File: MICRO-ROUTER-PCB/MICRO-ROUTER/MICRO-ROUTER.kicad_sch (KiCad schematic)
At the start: 72 parts, among them J2 USB_A, J3 USB_C_Receptacle_USB2.0_16P, J4 Battery Connector, J5 SPI Header, J6 GPIO Header, J7 RJ45 5-2301996-6, Q1 FS8205A, SW2 8Devices Reset, SW3 UART Reset, U1 TP4056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

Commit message: fixed reg
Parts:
- removed C9: 10uf, Capacitor_SMD:C_0603_1608Metric, symbol Device:C
- added L2: 4.7uf, Custom Footprints:INDPM5752X300N, symbol Device:L
- added U5: XC9141A50DMR-G, Custom Footprints:XC8107AC20MR-G, symbol Custom Symbols:XC9142B33DMR-G
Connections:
- net +5V: now also C7.1, U5.4 (Vout)
- net GND: now also U5.2 (GND)
- net V-UNREG: now also L2.2, U5.3 (BAT); no longer C7.1
- net V-UNREG SW: now reaches S1.2 (COM), U2.1 (CE)
- net V-UNREG SW: now also U5.1 (CE)
- new net: L2.1, U5.5 (LX)
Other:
- moved on the sheet: C1, C8, L1, S1, U2

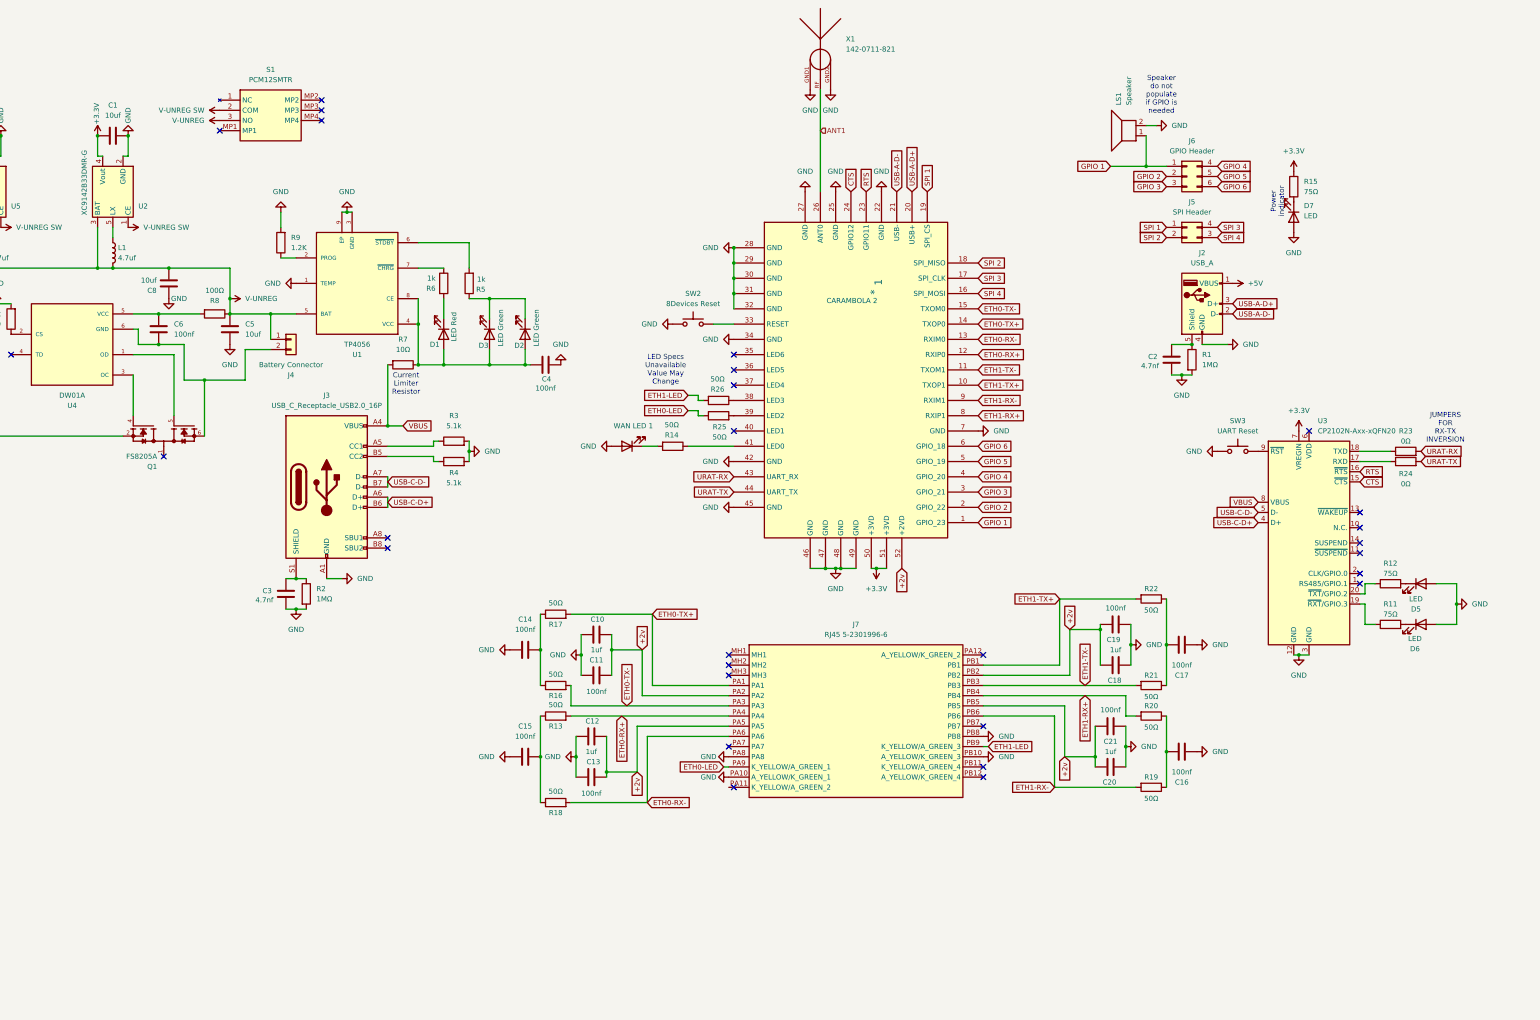
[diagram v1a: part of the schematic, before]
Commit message: -fixed all open issues in the schematic
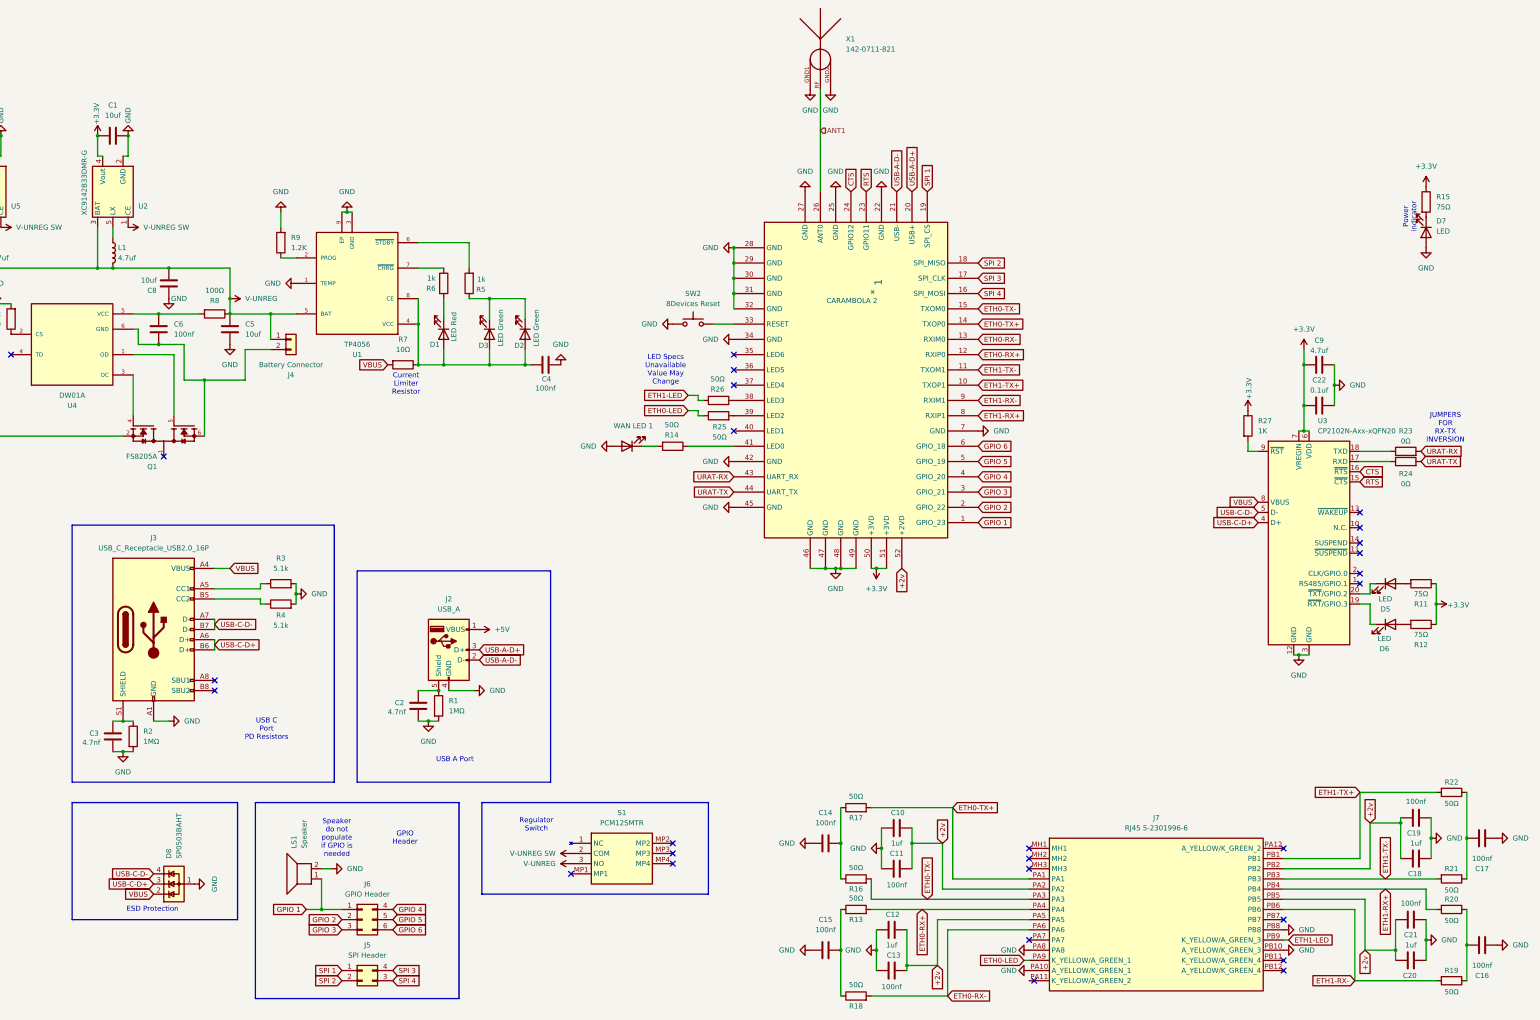
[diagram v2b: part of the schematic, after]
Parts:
- removed SW3: UART Reset, Button_Switch_THT:SW_PUSH_6mm, symbol Switch:SW_Push
- added C22: 0.1uf, symbol Device:C
- added C9: 4.7uf, symbol Device:C
- added D8: SP0503BAHT, Package_TO_SOT_SMD:SOT-143, symbol Power_Protection:SP0503BAHT
- added R27: 1K, Resistor_SMD:R_0603_1608Metric_Pad0.98x0.95mm_HandSolder, symbol Device:R
- J4: value Battery Connector -> Battery Connector
- U2: value XC9142B33DMR-G -> XC9142B33DMR-G
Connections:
- net +3.3V: now also R11.1, R12.1, U3.6 (VDD), C22.1, C9.1, R27.1
- net CTS: now also U3.16 (~{RTS}); no longer U3.15 (~{CTS})
- net GND: now also C22.2, C9.2, D8.1 (A); no longer D5.2 (A), D6.2 (A)
- net RTS: now also U3.15 (~{CTS}); no longer U3.16 (~{RTS})
- net USB-C-D+: now also D8.3 (K)
- net USB-C-D-: now also D8.4 (K)
- net VBUS: now also D8.2 (K)
- net at U3.9 (~{RST}): now also R27.2
- net at U3.19 (~{RXT}/GPIO.3): now also D6.1 (K); no longer R11.1
- net at R11.2: now also D5.2 (A); no longer D6.1 (K)
- net at U3.20 (~{TXT}/GPIO.2): now also D5.1 (K); no longer R12.1
- net at R12.2: now also D6.2 (A); no longer D5.1 (K)
- no-connect marks 28 -> 27
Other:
- note added: "ESD Protection"
- note added: "GPIO Header"
- note added: "Regulator Switch"
- note added: "USB A Port"
- note added: "USB C Port PD Resistors"
- moved on the sheet: C10, C11, C12, C13, C14, C15, C16, C17, C18, C19, C2, C20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

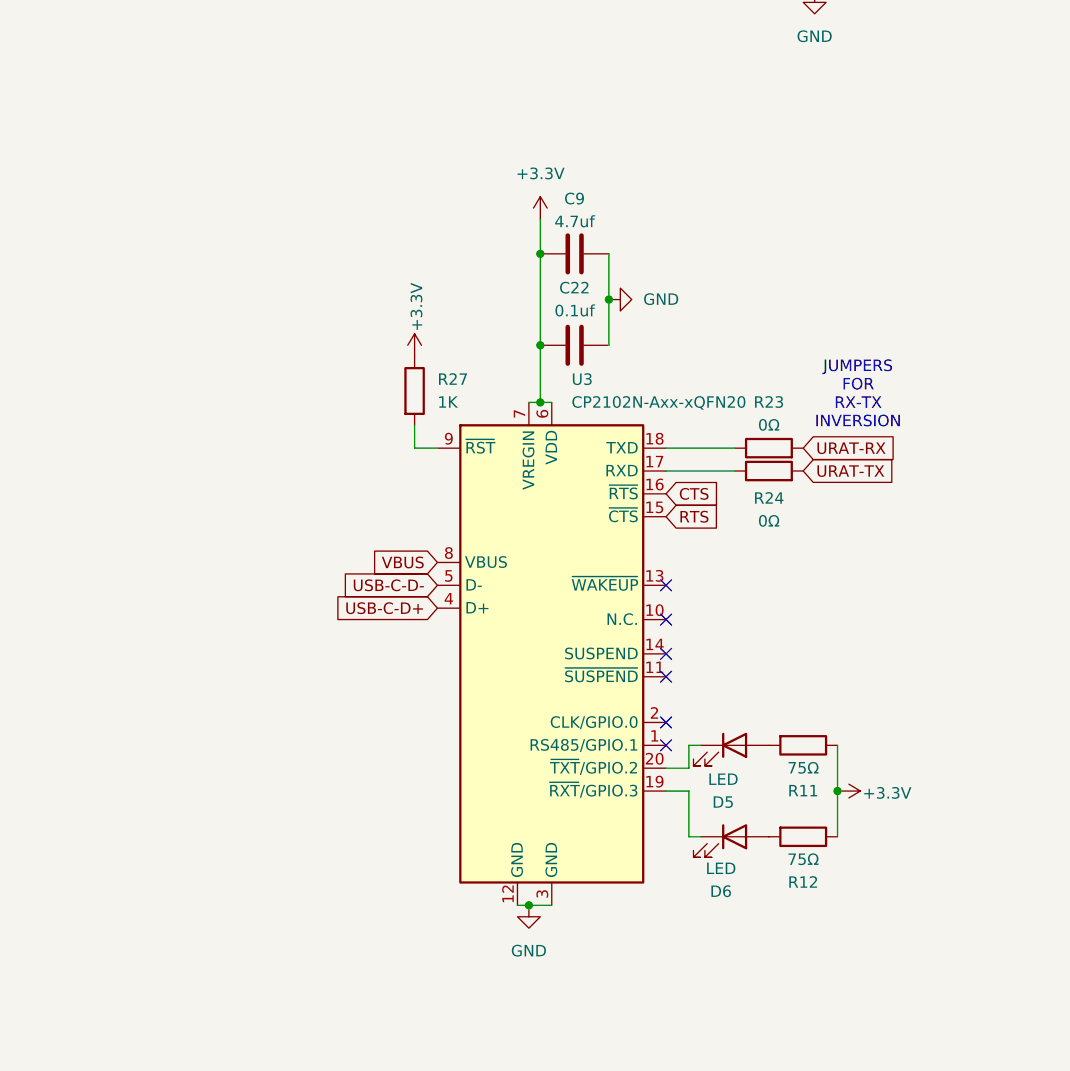
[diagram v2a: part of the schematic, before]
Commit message: -Fixed the ttl adapter (this time should be right)
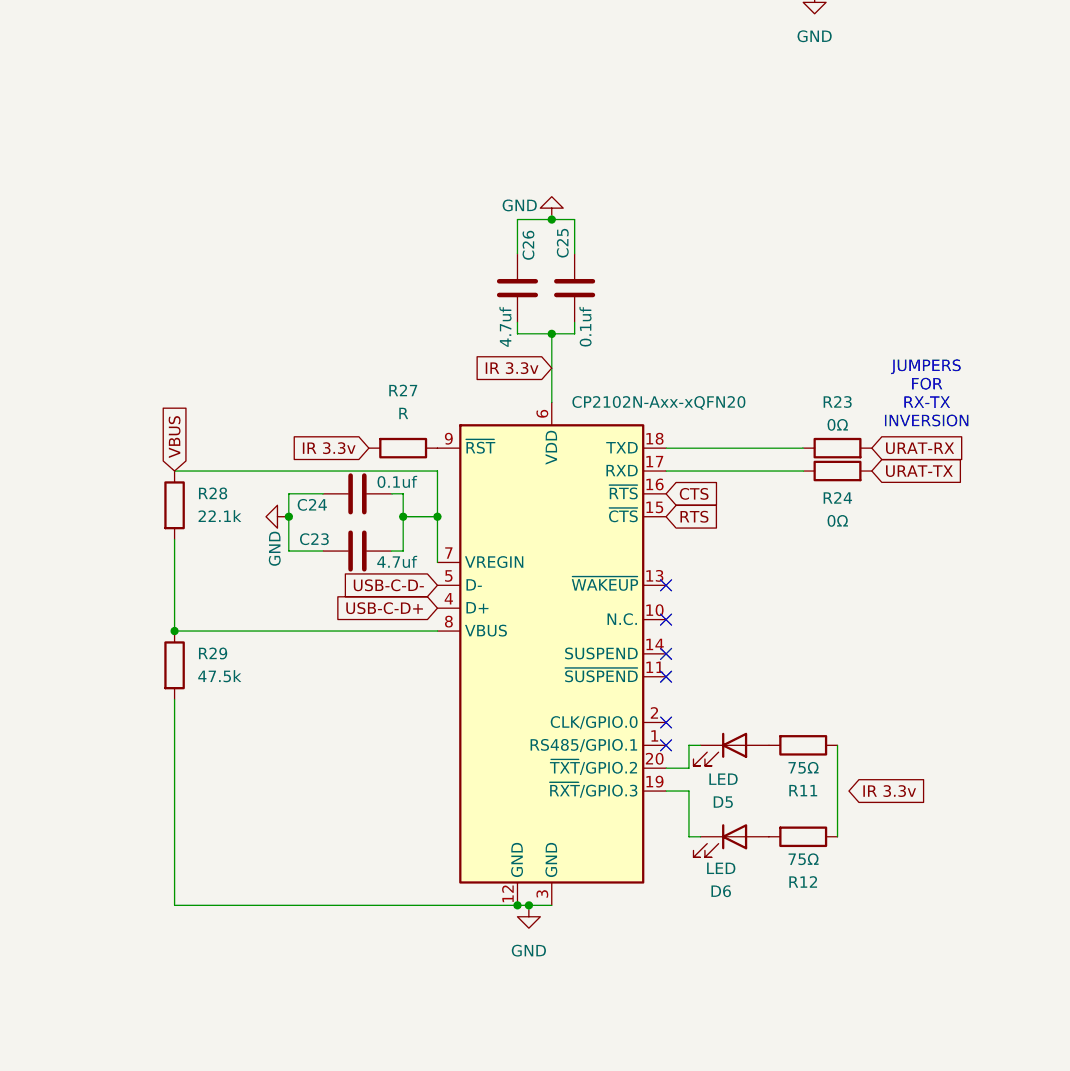
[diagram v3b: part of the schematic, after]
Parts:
- removed C22: 0.1uf, symbol Device:C
- removed C9: 4.7uf, symbol Device:C
- added C23, C26: 4.7uf, symbol Device:C
- added C24, C25: 0.1uf, symbol Device:C
- added R28: 22.1k, symbol Device:R
- added R29: 47.5k, symbol Device:R
- R27: value 1K -> R; footprint Resistor_SMD:R_0603_1608Metric_Pad0.98x0.95mm_HandSolder -> (none)
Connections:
- net +3.3V: no longer R11.1, R12.1, R27.1, U3.6 (VDD), U3.7 (VREGIN)
- net GND: now also C23.2, C24.2, C25.2, C26.2, R29.2
- net VBUS: now also U3.7 (VREGIN), C23.1, C24.1, R28.1; no longer U3.8 (VBUS)
- net at U3.9 (~{RST}): now also R27.1; no longer R27.2
- new net: R28.2, R29.1, U3.8 (VBUS)
- new net: R11.1, R12.1
- new net IR 3.3v: C25.1, C26.1, R27.2, U3.6 (VDD)
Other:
- moved on the sheet: R23, R24
